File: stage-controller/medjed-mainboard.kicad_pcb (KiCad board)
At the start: 4 copper layers, 125 x 56.9 mm, 104 parts, among them J1 Barrel_Jack, J2 ESTOP terminal, J3 Conn_01x04_Pin, SW2 ESTOP switch, U1 P78E-1000, U10 TCAN330, U11 teensy 4.1, U12 MIC5317-3.3, U13 MIC5317-1.8, U17 TMC4361A-LA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

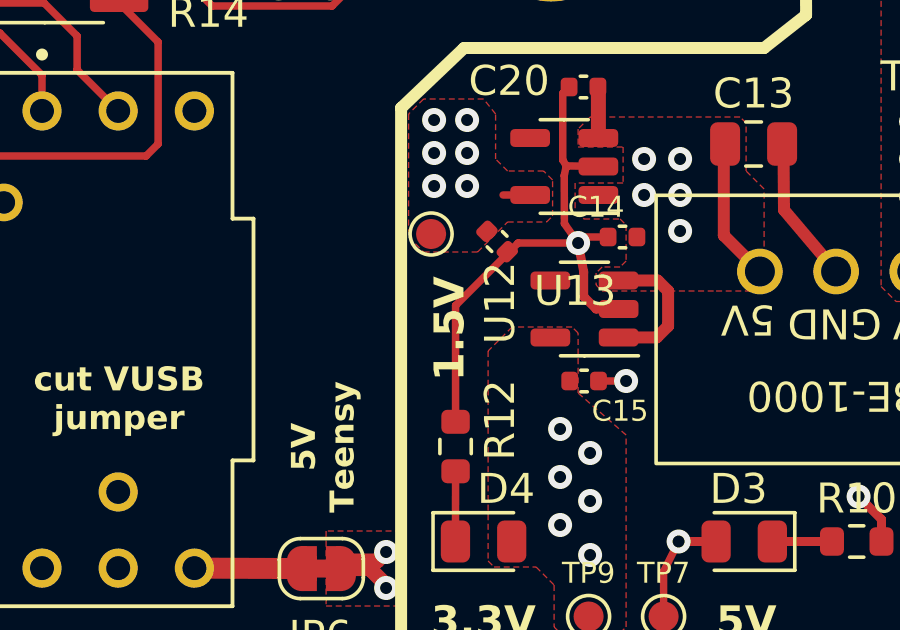
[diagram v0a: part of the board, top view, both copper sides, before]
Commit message: fix silkscreen error
Silkscreen labelled the 1.8V net as 1.5V, which is confusing. Fixed by editing the silkscreen label.
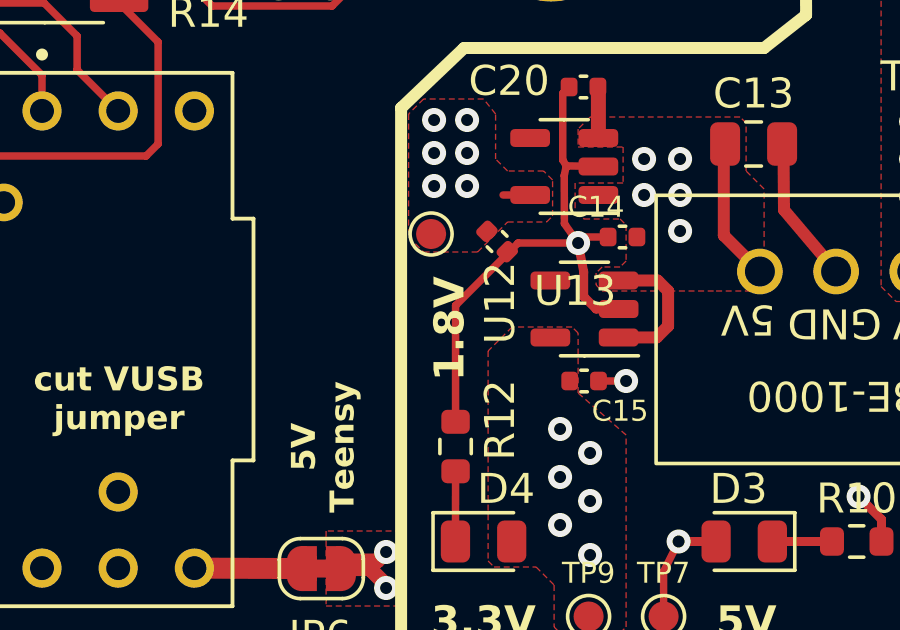
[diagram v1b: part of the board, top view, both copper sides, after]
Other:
- board text added: "1.8V"
- board text removed: "1.5V"
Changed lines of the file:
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@@
     (effects (font (size 2 2) (thickness 0.35) bold) (justify bottom))
   )
-  (gr_text "1.5V\n" (at 117.7 67.4 90) (layer "F.SilkS" knockout)
+  (gr_text "1.8V\n" (at 117.7 67.4 90) (layer "F.SilkS" knockout)
     (effects (font (size 1 1) (thickness 0.18) bold) (justify left bottom))
   )

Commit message: fix Teensy 4.1 footprint
Original footprint had through hole pads that were too small (0.8mm diameter). New ones are bigger to accomodate common pin headers.
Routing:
- net MISO: track 99.9 -> 99.3 mm

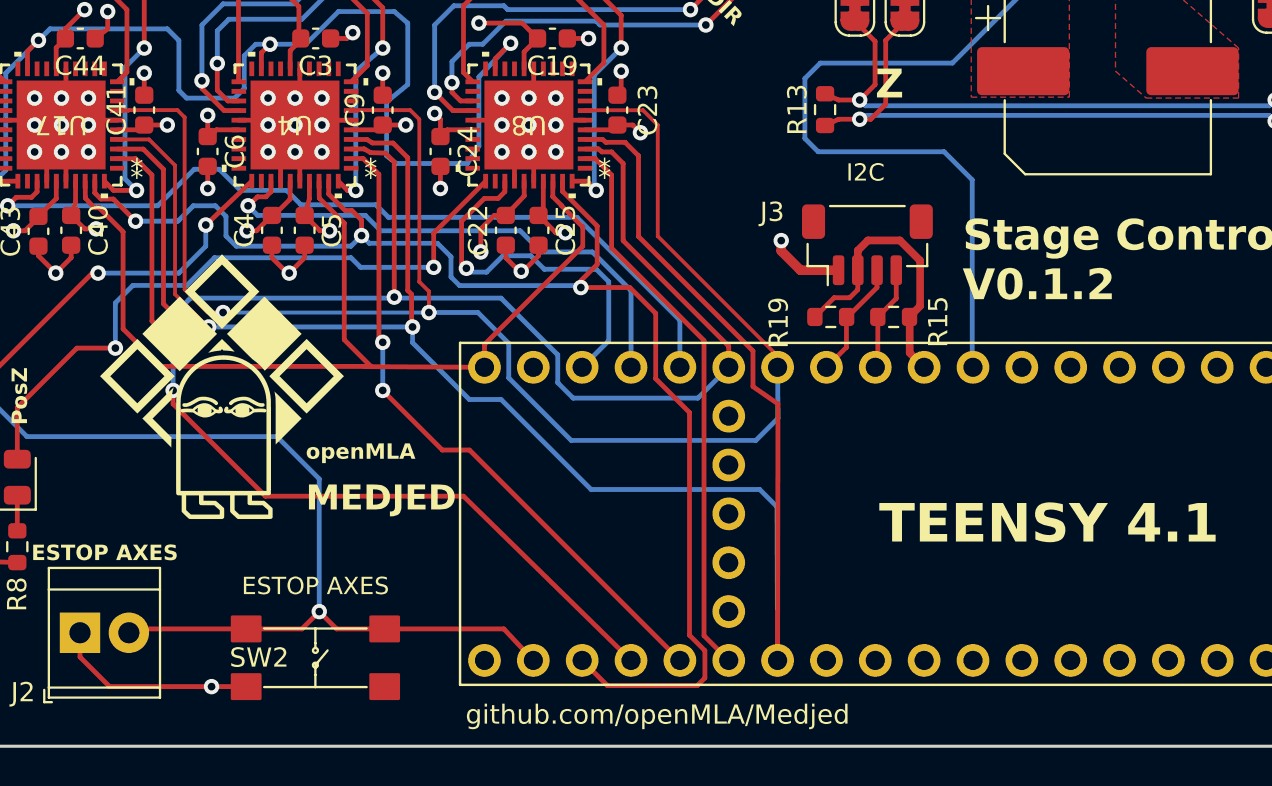
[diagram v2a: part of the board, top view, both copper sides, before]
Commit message: Fix Clock pin and MISO/MOSI error
The TeensyCLK signal was routed to a pin on the Teensy 4.1 that did not support PWM. Now fixed. MOSI and MISO of SPI interface were flipped around by mistake. Now in correct orientation and should allow SPI communication (tested with messy wiring).
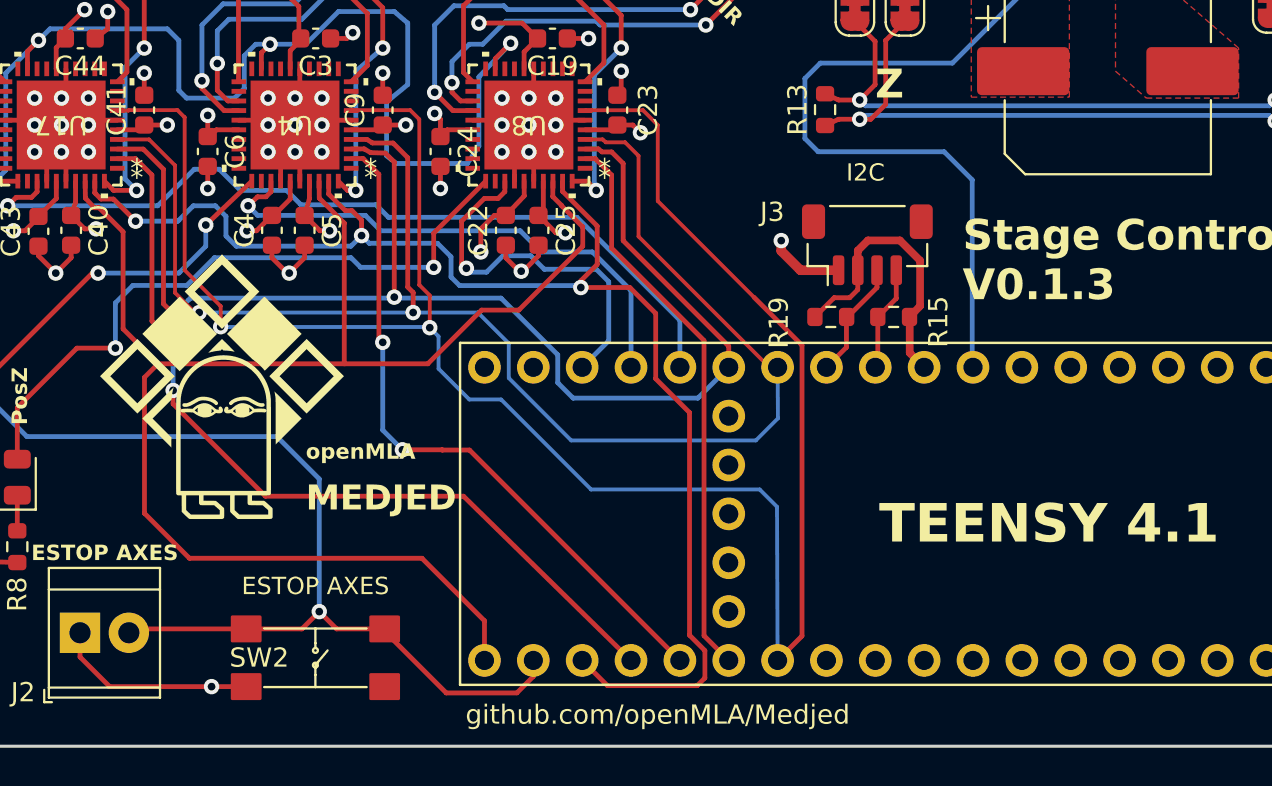
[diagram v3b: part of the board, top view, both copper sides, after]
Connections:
- U11 pad 32: TeensyCLK -> unconnected-(U11-OUT1B-Pad32)
- U11 pad 33: unconnected-(U11-MCLK2-Pad33) -> TeensyCLK
- U17 pad 4: MISO -> MOSI
- U17 pad 7: MOSI -> MISO
- U4 pad 4: MISO -> MOSI
- U4 pad 7: MOSI -> MISO
- U8 pad 4: MISO -> MOSI
- U8 pad 7: MOSI -> MISO
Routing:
- net TeensyCLK: track 51.4 -> 80.0 mm
- net MISO: track 99.3 -> 107.5 mm
- net MOSI: track 84.2 -> 77.7 mm
- net ESTOP: track 117.7 -> 119.7 mm
- net CS_Y: track 34.4 -> 35.6 mm
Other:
- board text added: "Stage Controller V0.1.3"
- board text removed: "Stage Controller V0.1.2"

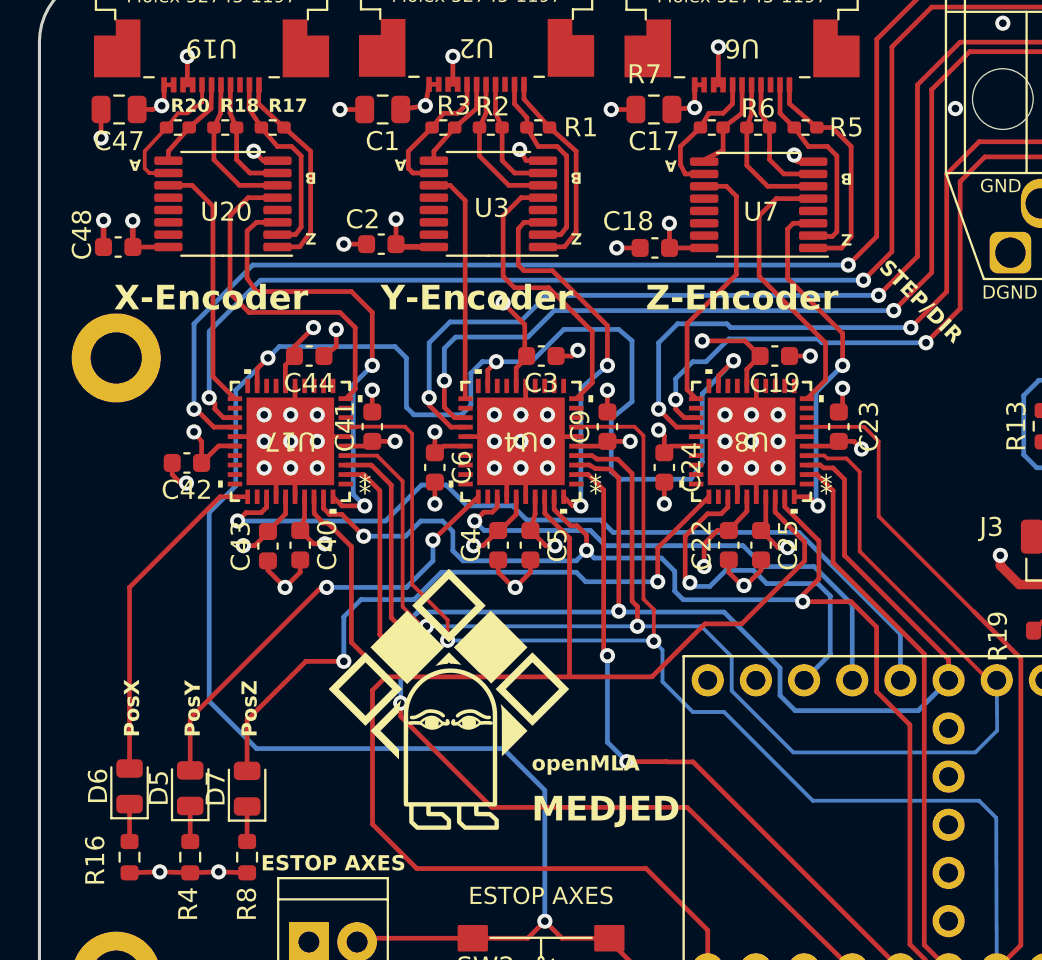
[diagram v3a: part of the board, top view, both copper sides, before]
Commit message: Removed differential line receivers
During design of the board I did not realise that the TMC4631 already has this built in (I had different motion controllers before). So the AM26LS32A ICs should not be needed. Removed these and rerouted the board.
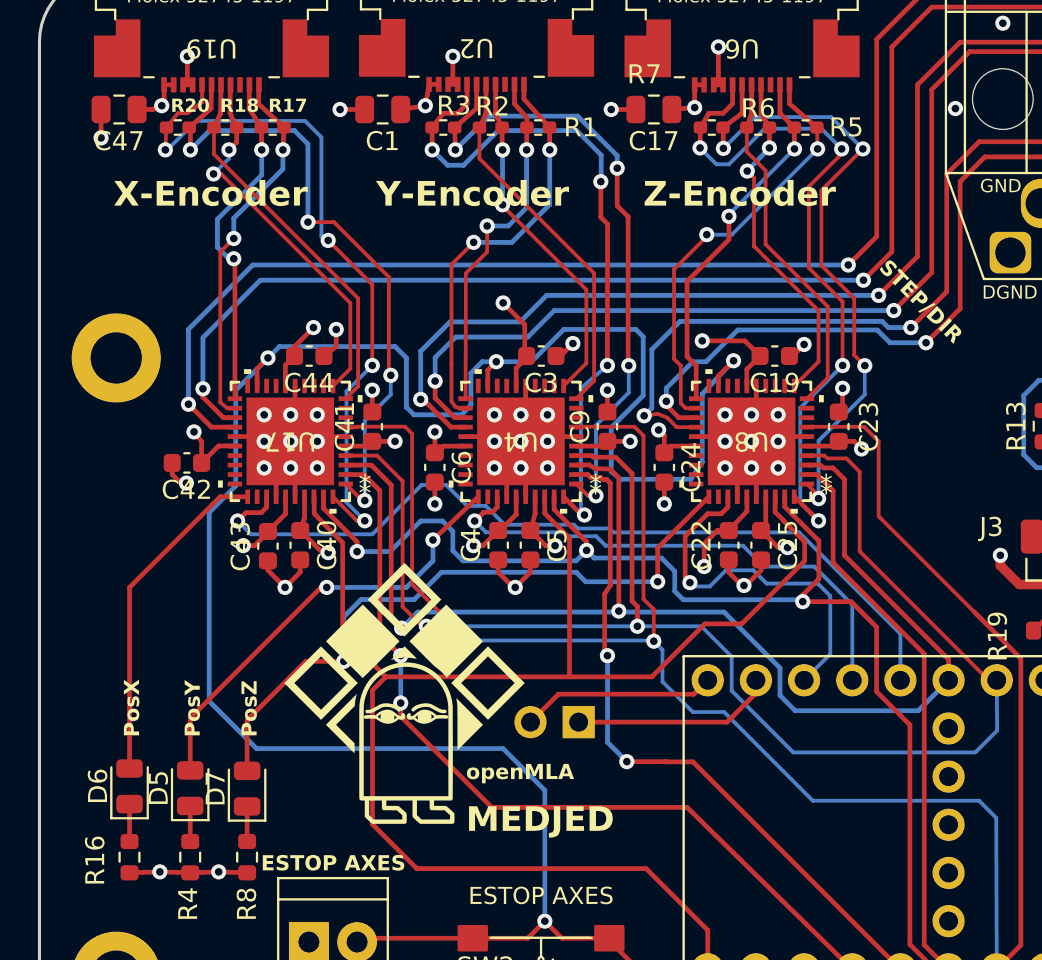
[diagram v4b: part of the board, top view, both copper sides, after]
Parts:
- removed C18, C2, C48: 100nF, Capacitor_SMD:C_0603_1608Metric
- removed U20, U3, U7: ~, medjed-mainboard:TSSOP-16-AM26LS32A
- added J4: GPIO, Connector_PinSocket_2.54mm:PinSocket_1x02_P2.54mm_Vertical, F.Cu at (43.4, 60.6)
- J3: value Conn_01x04_Pin -> Stemma QT
- moved G*** 2.36 mm to (34.2, 59.1)
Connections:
- R1 pad 1: /Axis Y/Z_Z- -> /Axis Y/Z-
- R1 pad 2: /Axis Y/Z_Z+ -> /Axis Y/Z+
- R17 pad 1: /Axis X/Z_Z- -> /Axis X/Z-
- R17 pad 2: /Axis X/Z_Z+ -> /Axis X/Z+
- R18 pad 1: /Axis X/Z_B- -> /Axis X/B-
- R18 pad 2: /Axis X/Z_B+ -> /Axis X/B+
- R2 pad 1: /Axis Y/Z_B- -> /Axis Y/B-
- R2 pad 2: /Axis Y/Z_B+ -> /Axis Y/B+
- R20 pad 1: /Axis X/Z_A- -> /Axis X/A-
- R20 pad 2: /Axis X/Z_A+ -> /Axis X/A+
- R3 pad 1: /Axis Y/Z_A- -> /Axis Y/A-
- R3 pad 2: /Axis Y/Z_A+ -> /Axis Y/A+
- R5 pad 1: /Axis Z/Z_Z- -> /Axis Z/Z-
- R5 pad 2: /Axis Z/Z_Z+ -> /Axis Z/Z+
- R6 pad 1: /Axis Z/Z_B- -> /Axis Z/B-
- R6 pad 2: /Axis Z/Z_B+ -> /Axis Z/B+
- R7 pad 1: /Axis Z/Z_A- -> /Axis Z/A-
- R7 pad 2: /Axis Z/Z_A+ -> /Axis Z/A+
- U11 pad 31: unconnected-(U11-CTX3-Pad31) -> Pin 1
- U11 pad 32: unconnected-(U11-OUT1B-Pad32) -> Pin 2
- U17 pad 1: (no net) -> /Axis X/A-
- U17 pad 10: /Axis X/B -> /Axis X/B+
- U17 pad 11: (no net) -> /Axis X/B-
- U17 pad 21: /Axis X/N -> /Axis X/Z+
- U17 pad 22: (no net) -> /Axis X/Z-
- U17 pad 40: /Axis X/A -> /Axis X/A+
- U19 pad 10: /Axis X/Z_Z+ -> /Axis X/Z+
- U19 pad 11: /Axis X/Z_Z- -> /Axis X/Z-
- U19 pad 5: /Axis X/Z_A+ -> /Axis X/A+
- U19 pad 6: /Axis X/Z_A- -> /Axis X/A-
- U19 pad 7: /Axis X/Z_B+ -> /Axis X/B+
- U19 pad 8: /Axis X/Z_B- -> /Axis X/B-
- U2 pad 10: /Axis Y/Z_Z+ -> /Axis Y/Z+
- U2 pad 11: /Axis Y/Z_Z- -> /Axis Y/Z-
- U2 pad 5: /Axis Y/Z_A+ -> /Axis Y/A+
- U2 pad 6: /Axis Y/Z_A- -> /Axis Y/A-
- U2 pad 7: /Axis Y/Z_B+ -> /Axis Y/B+
- U2 pad 8: /Axis Y/Z_B- -> /Axis Y/B-
- U4 pad 1: (no net) -> /Axis Y/A-
- U4 pad 10: /Axis Y/B -> /Axis Y/B+
- U4 pad 11: (no net) -> /Axis Y/B-
- U4 pad 21: /Axis Y/N -> /Axis Y/Z+
- U4 pad 22: (no net) -> /Axis Y/Z-
- U4 pad 40: /Axis Y/A -> /Axis Y/A+
- U6 pad 10: /Axis Z/Z_Z+ -> /Axis Z/Z+
- U6 pad 11: /Axis Z/Z_Z- -> /Axis Z/Z-
- U6 pad 5: /Axis Z/Z_A+ -> /Axis Z/A+
- U6 pad 6: /Axis Z/Z_A- -> /Axis Z/A-
- U6 pad 7: /Axis Z/Z_B+ -> /Axis Z/B+
- U6 pad 8: /Axis Z/Z_B- -> /Axis Z/B-
- U8 pad 1: (no net) -> /Axis Z/A-
- U8 pad 10: /Axis Z/B -> /Axis Z/B+
- U8 pad 11: (no net) -> /Axis Z/B-
- U8 pad 21: /Axis Z/N -> /Axis Z/Z+
- U8 pad 22: (no net) -> /Axis Z/Z-
- U8 pad 40: /Axis Z/A -> /Axis Z/A+
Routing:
- net /Axis X/A+: track 0.00 -> 38.5 mm, vias 0 -> 4
- net /Axis Z/A+: track 0.00 -> 37.7 mm, vias 0 -> 4
- net /Axis Y/A+: track 0.00 -> 36.9 mm, vias 0 -> 4
- net /Axis Z/A-: track 0.00 -> 35.1 mm, vias 0 -> 4
- net /Axis X/A-: track 0.00 -> 34.7 mm, vias 0 -> 4
- net /Axis Y/A-: track 0.00 -> 34.7 mm, vias 0 -> 4
- net /Axis X/A: track 24.4 -> 0.00 mm, vias 2 -> 0
- net /Axis Z/Z-: track 0.00 -> 22.6 mm, vias 0 -> 2
- net /Axis Y/Z-: track 0.00 -> 21.6 mm, vias 0 -> 2
- net /Axis Y/A: track 20.6 -> 0.00 mm, vias 2 -> 0
- net /Axis X/B-: track 0.00 -> 20.1 mm, vias 0 -> 2
- net /Axis X/B+: track 0.00 -> 20.0 mm
- net /Axis X/Z-: track 0.00 -> 19.6 mm, vias 0 -> 2
- net /Axis Y/B+: track 0.00 -> 19.5 mm
- net /Axis Z/Z+: track 0.00 -> 19.5 mm, vias 0 -> 2
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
